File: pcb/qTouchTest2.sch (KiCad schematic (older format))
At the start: 40 parts, among them CON1 AVR-ISP-6, J1 USB-MINI-B, K1 CONN_3, P1 CONN_1, P2 CONN_1, P3 CONN_1, P6 CONN_1, P7 CONN_1, P8 CONN_1, P9 CONN_1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

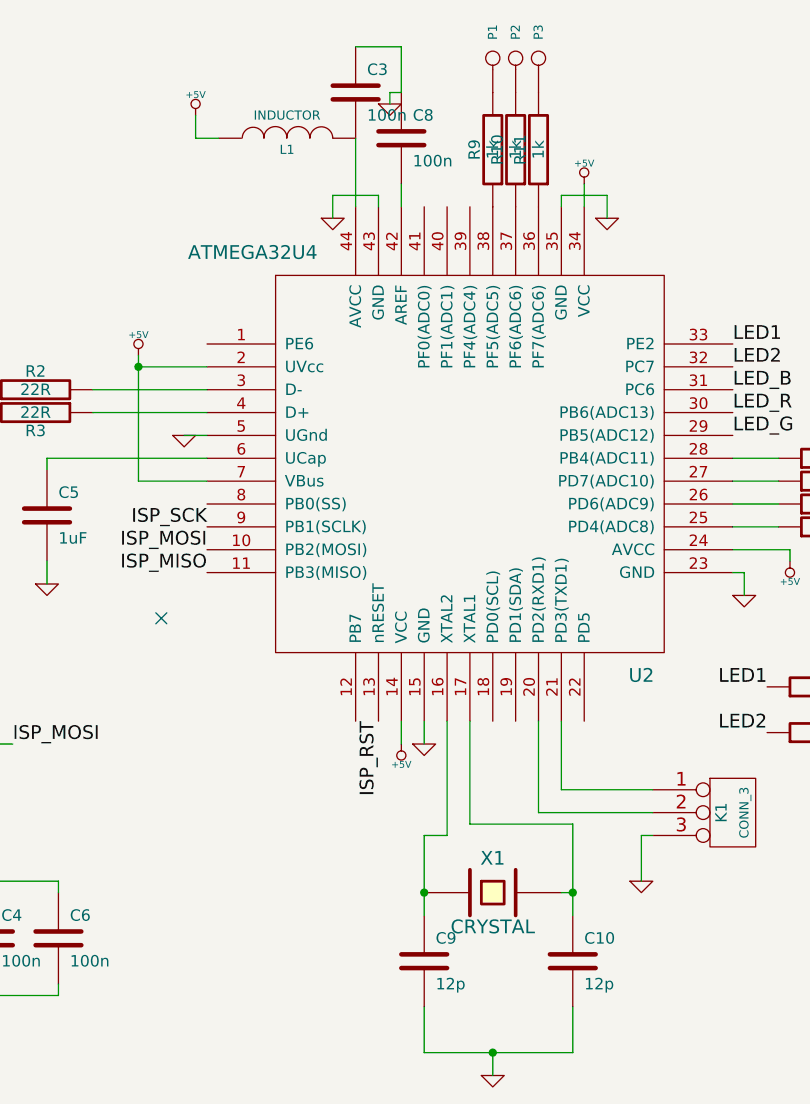
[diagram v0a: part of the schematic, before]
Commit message: adding ferrite bead and crystal info
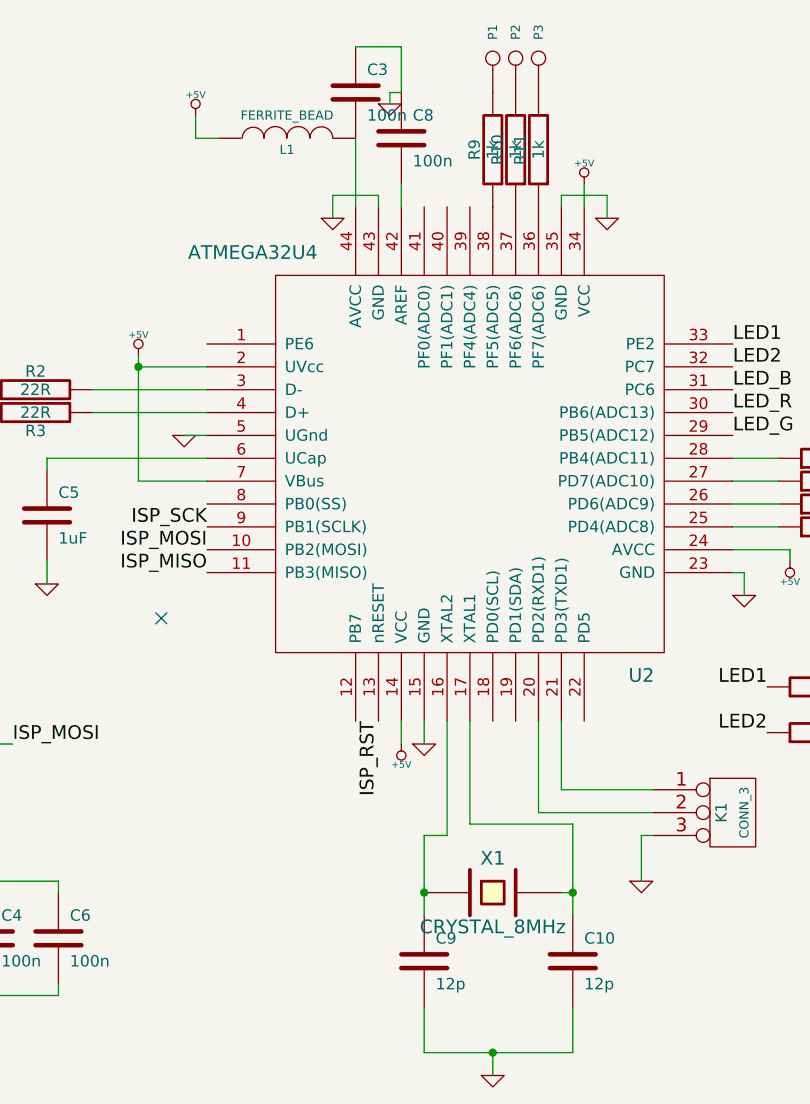
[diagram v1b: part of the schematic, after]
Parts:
- L1: value INDUCTOR -> FERRITE_BEAD
- X1: value CRYSTAL -> CRYSTAL_8MHz
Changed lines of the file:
@@
-EESchema Schematic File Version 2  date Thu 28 Mar 2013 16:16:28 GMT
+EESchema Schematic File Version 2  date Thu 28 Mar 2013 16:25:18 GMT
 LIBS:power
 LIBS:device
@@
 Sheet 1 1
 Title ""
-Date "27 mar 2013"
+Date "28 mar 2013"
 Rev ""
 Comp ""
@@
 P 5100 1950
 F 0 "L1" V 5050 1950 40  0000 C CNN
-F 1 "INDUCTOR" V 5200 1950 40  0000 C CNN
+F 1 "FERRITE_BEAD" V 5200 1950 40  0000 C CNN
 F 2 "" H 5100 1950 60  0001 C CNN
 F 3 "" H 5100 1950 60  0001 C CNN
@@
 P 6000 5250
 F 0 "X1" H 6000 5400 60  0000 C CNN
-F 1 "CRYSTAL" H 6000 5100 60  0000 C CNN
+F 1 "CRYSTAL_8MHz" H 6000 5100 60  0000 C CNN
 F 2 "" H 6000 5250 60  0001 C CNN
 F 3 "" H 6000 5250 60  0001 C CNN

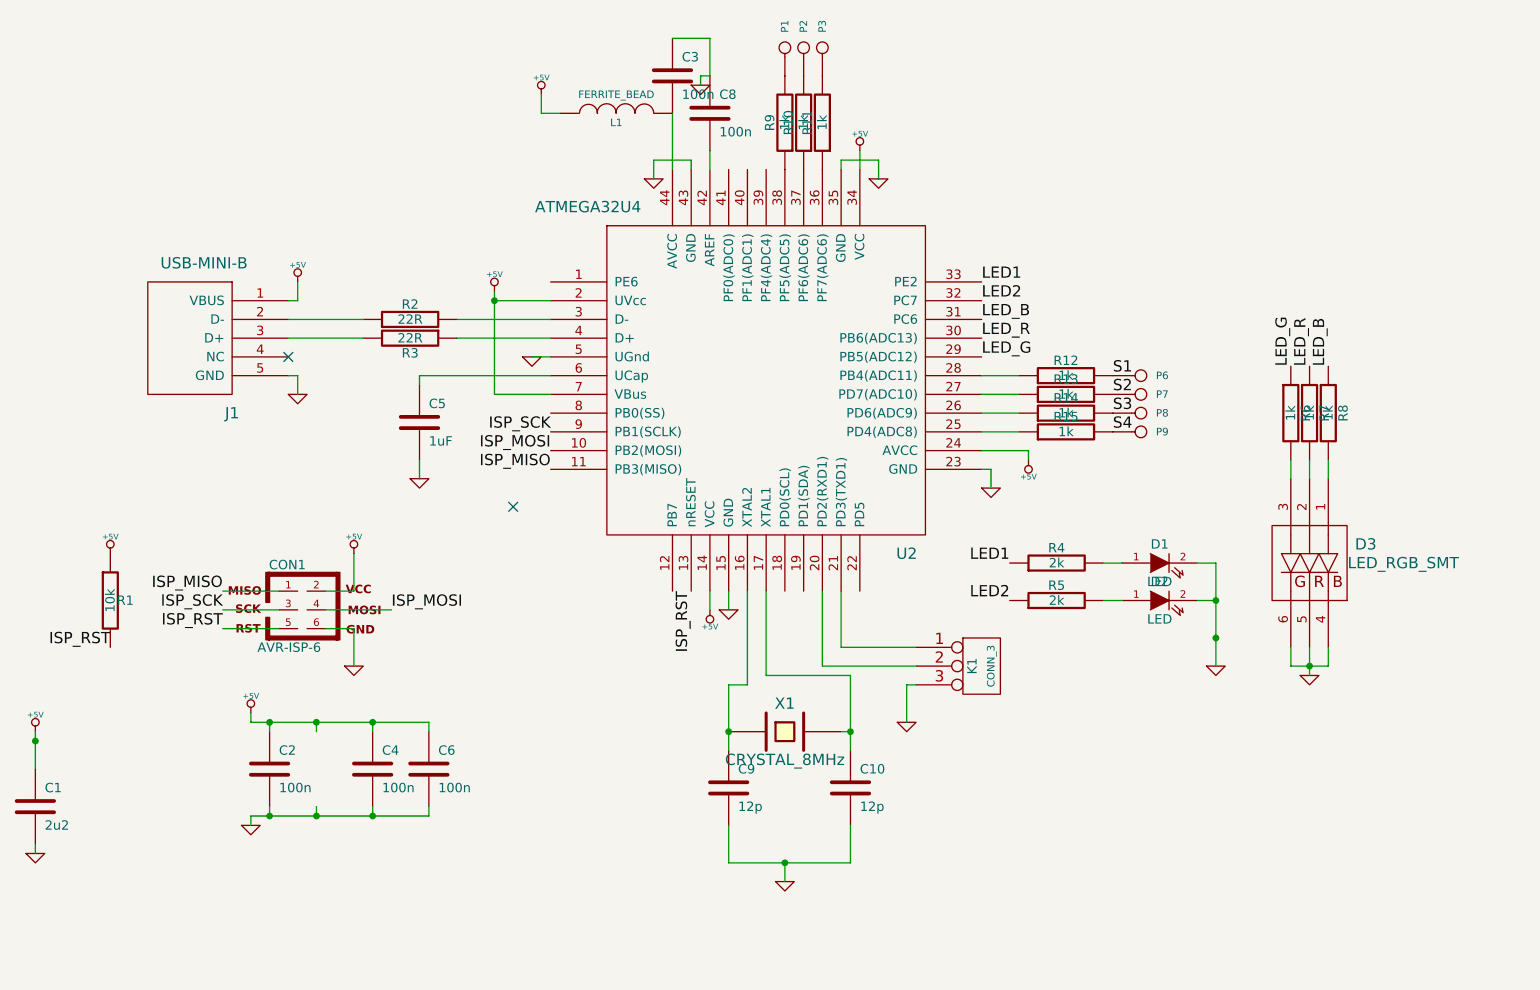
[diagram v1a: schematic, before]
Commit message: adding colour info to LEDs
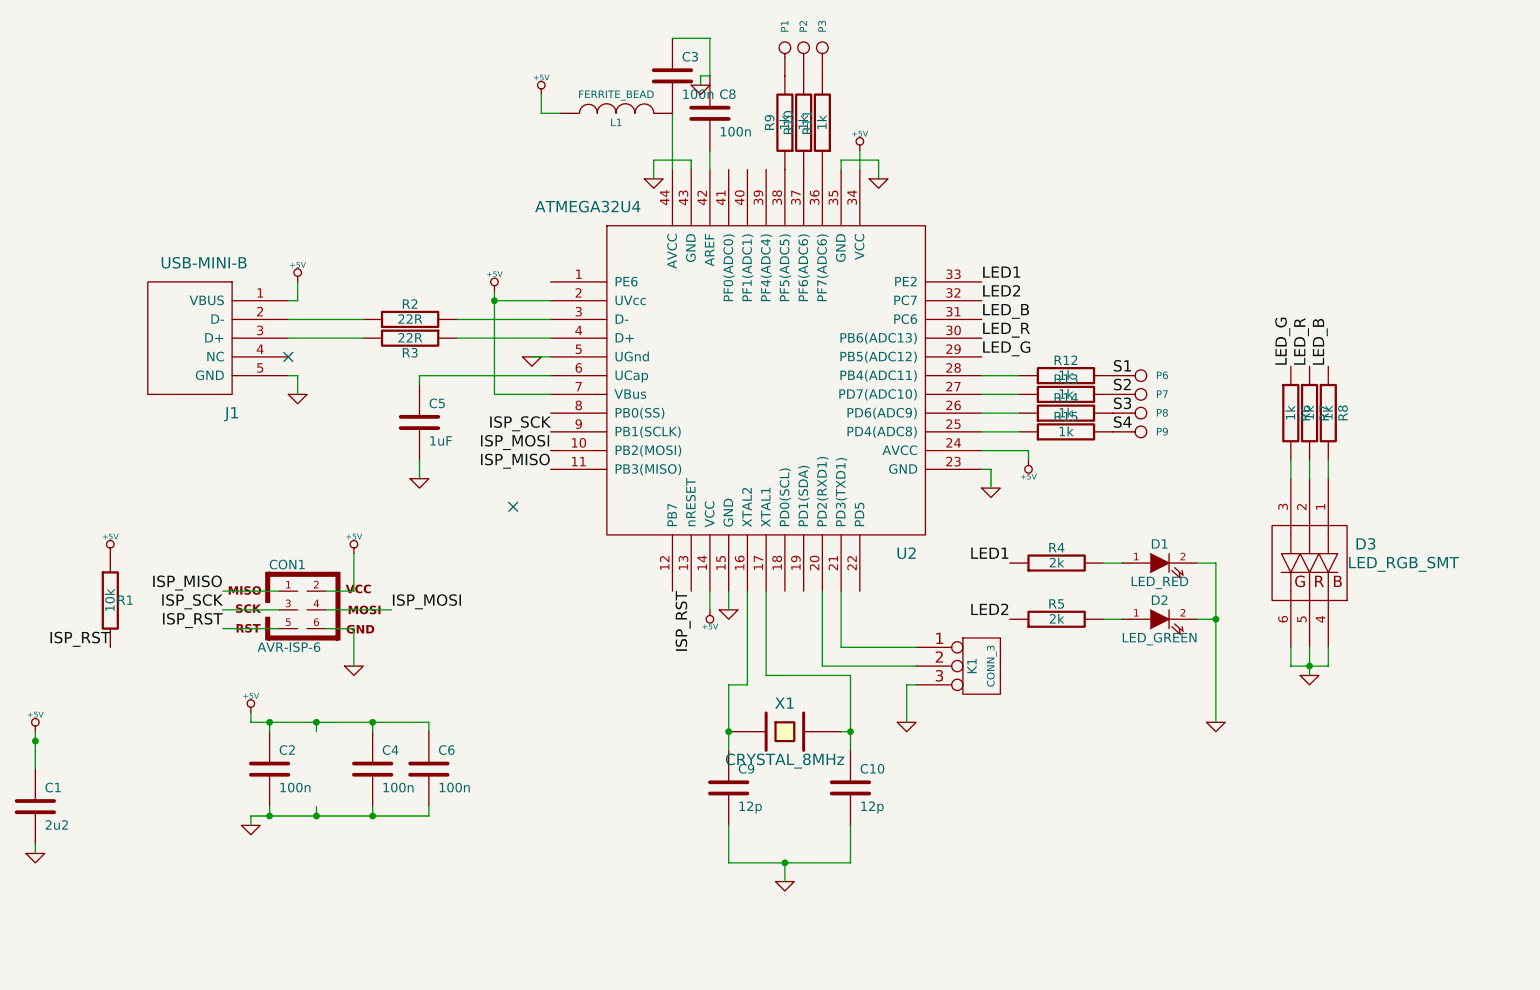
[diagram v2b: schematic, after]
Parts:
- D1: value LED -> LED_RED
- D2: value LED -> LED_GREEN
- J1: Distributer  (none) -> Farnell; Distributer no. (none) -> 2112367; Manufacturer (none) -> FCI; Manufacturer no. (none) -> 10033526-N3212MLF
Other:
- moved on the sheet: D2, R5
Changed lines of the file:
@@
-EESchema Schematic File Version 2  date Thu 28 Mar 2013 16:25:18 GMT
+EESchema Schematic File Version 2  date Thu 28 Mar 2013 16:47:26 GMT
 LIBS:power
 LIBS:device
@@
 	8800 3800 8800 3900
 Wire Wire Line
-	8900 4900 8700 4900
+	8700 4900 8900 4900
 Wire Wire Line
 	8900 4900 8900 4800
@@
 	3500 5250 3500 5200
 Wire Wire Line
-	4100 5250 4100 5200
-Wire Wire Line
-	4100 5200 3150 5200
+	4100 5200 4100 5250
+Wire Wire Line
+	3150 5200 4100 5200
 Wire Wire Line
 	3150 5200 3150 5150
@@
 Connection ~ 6350 5250
 Wire Wire Line
-	6350 5350 6350 4950
+	6350 4950 6350 5350
 Wire Wire Line
 	6350 5250 6300 5250
@@
 Connection ~ 4450 2950
 Wire Wire Line
-	4750 3450 4450 3450
-Wire Wire Line
-	4450 3450 4450 2900
+	4450 3450 4750 3450
+Wire Wire Line
+	4450 2900 4450 3450
 Wire Wire Line
 	3350 2950 3400 2950
@@
 	2000 5900 2000 5850
 Wire Wire Line
-	7700 4550 7800 4550
-Connection ~ 8300 4750
+	7700 4650 7800 4650
 Wire Wire Line
 	8200 4350 8300 4350
 Wire Wire Line
-	8300 4350 8300 4900
+	8300 4350 8300 5200
 Wire Wire Line
 	4250 3050 4750 3050
@@
 	4750 3150 4250 3150
 Wire Wire Line
-	8200 4550 8300 4550
-Connection ~ 8300 4550
+	8200 4650 8300 4650
+Connection ~ 8300 4650
 Wire Wire Line
 	7800 4350 7700 4350
@@
 	7100 3850 7100 3950
 Wire Wire Line
-	4100 5700 3150 5700
+	3150 5700 4100 5700
 Wire Wire Line
 	4100 5700 4100 5650
@@
 Text Label 7050 2850 0    60   ~ 0
 LED1
-Text Label 7200 4550 2    60   ~ 0
+Text Label 7200 4650 2    60   ~ 0
 LED2
 Text Label 7200 4350 2    60   ~ 0
@@
 L GND #PWR025
 U 1 1 4F967382
-P 8300 4900
-F 0 "#PWR025" H 8300 4900 30  0001 C CNN
-F 1 "GND" H 8300 4830 30  0001 C CNN
-F 2 "" H 8300 4900 60  0001 C CNN
-F 3 "" H 8300 4900 60  0001 C CNN
-	1    8300 4900
+P 8300 5200
+F 0 "#PWR025" H 8300 5200 30  0001 C CNN
+F 1 "GND" H 8300 5130 30  0001 C CNN
+F 2 "" H 8300 5200 60  0001 C CNN
+F 3 "" H 8300 5200 60  0001 C CNN
+	1    8300 5200
 	1    0    0    -1
 $EndComp
@@
 L LED D2
 U 1 1 4F96737F
-P 8000 4550
-F 0 "D2" H 8000 4650 50  0000 C CNN
-F 1 "LED" H 8000 4450 50  0000 C CNN
-F 2 "" H 8000 4550 60  0001 C CNN
-F 3 "" H 8000 4550 60  0001 C CNN
-	1    8000 4550
+P 8000 4650
+F 0 "D2" H 8000 4750 50  0000 C CNN
+F 1 "LED_GREEN" H 8000 4550 50  0000 C CNN
+F 2 "" H 8000 4650 60  0001 C CNN
+F 3 "" H 8000 4650 60  0001 C CNN
+	1    8000 4650
 	1    0    0    -1
 $EndComp
@@
 P 8000 4350
 F 0 "D1" H 8000 4450 50  0000 C CNN
-F 1 "LED" H 8000 4250 50  0000 C CNN
+F 1 "LED_RED" H 8000 4250 50  0000 C CNN
 F 2 "" H 8000 4350 60  0001 C CNN
 F 3 "" H 8000 4350 60  0001 C CNN
@@
 L R R5
 U 1 1 4F96735E
-P 7450 4550
-F 0 "R5" V 7530 4550 50  0000 C CNN
-F 1 "2k" V 7450 4550 50  0000 C CNN
-F 2 "" H 7450 4550 60  0001 C CNN
-F 3 "" H 7450 4550 60  0001 C CNN
-	1    7450 4550
+P 7450 4650
+F 0 "R5" V 7530 4650 50  0000 C CNN
+F 1 "2k" V 7450 4650 50  0000 C CNN
+F 2 "" H 7450 4650 60  0001 C CNN
+F 3 "" H 7450 4650 60  0001 C CNN
+	1    7450 4650
 	0    -1   -1   0
 $EndComp
@@
 F 2 "" H 3050 3550 60  0001 C CNN
 F 3 "" H 3050 3550 60  0001 C CNN
+F 4 "FCI" H 3050 3550 60  0001 C CNN "Manufacturer"
+F 5 "10033526-N3212MLF" H 3050 3550 60  0001 C CNN "Manufacturer no."
+F 6 "Farnell" H 3050 3550 60  0001 C CNN "Distributer "
+F 7 "2112367" H 3050 3550 60  0001 C CNN "Distributer no."
 	1    3050 3550
 	1    0    0    -1

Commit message: adding ferrite bead to AVCC on pin 24
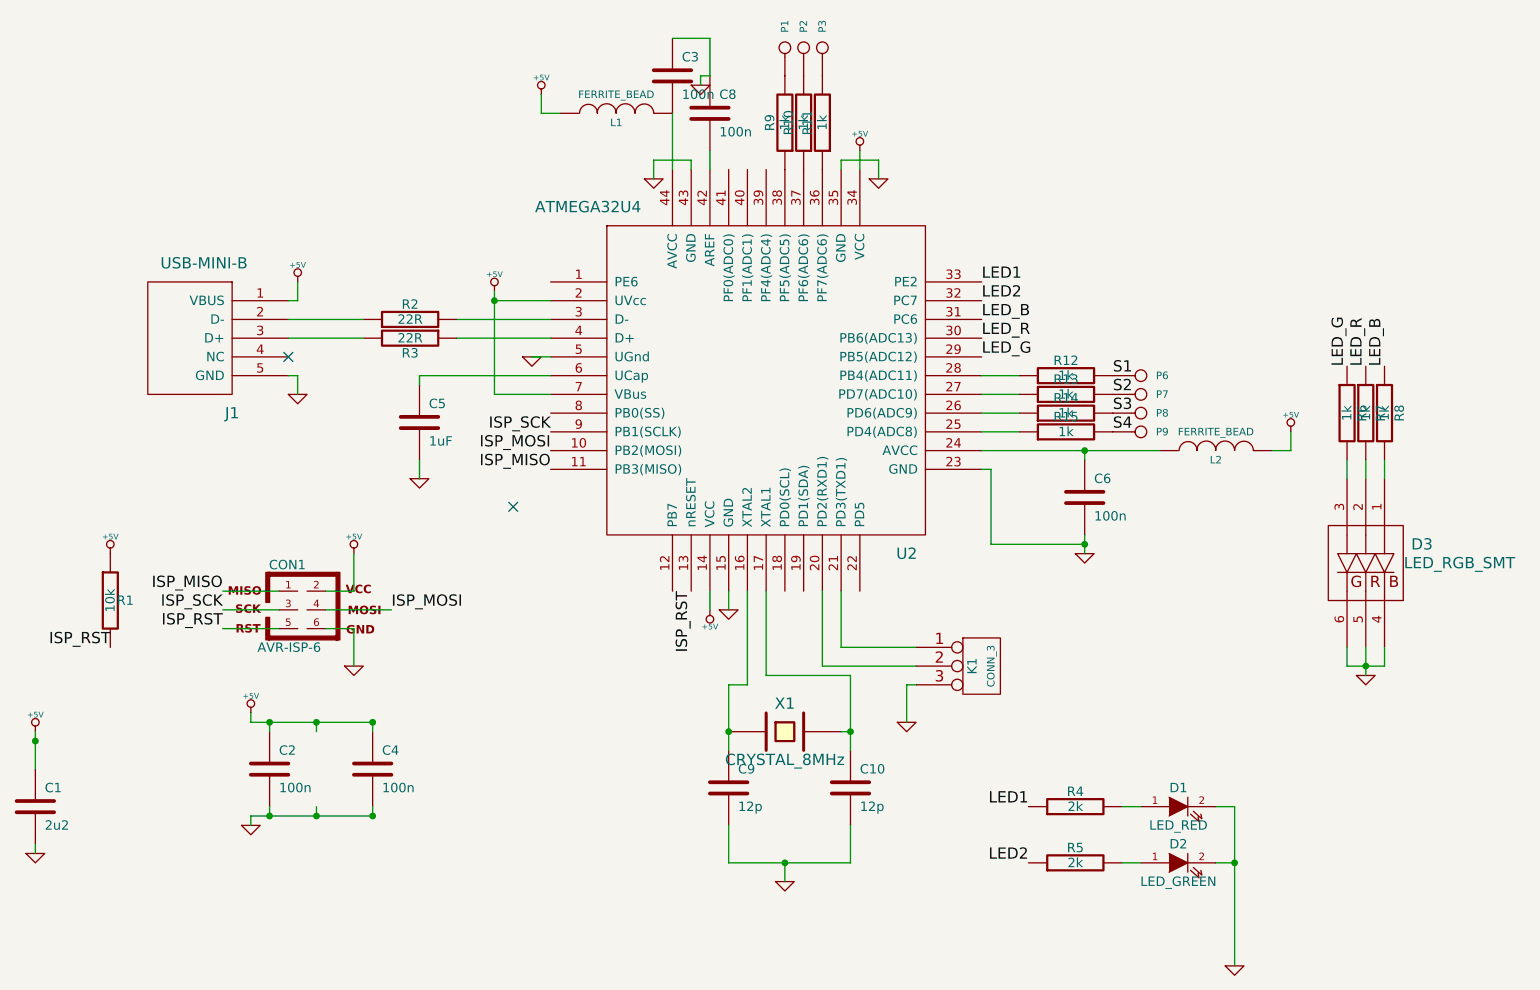
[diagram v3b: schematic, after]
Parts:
- added L2: FERRITE_BEAD, symbol INDUCTOR
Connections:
- net +5V: now also L2.2; no longer C6.1, U2.24 (AVCC)
- new net: C6.1, L2.1, U2.24 (AVCC)
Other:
- moved on the sheet: C6, D1, D2, D3, R4, R5, R6, R7, R8
